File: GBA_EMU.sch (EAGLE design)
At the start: 73 parts, among them J1 USB-MINIB-5PIN, J2 AVR_SPI, Q1 MOSFET-PCHANNEL, SW1 LEFT, SW2 RIGHT, SW3 PWR_SWITCH, U2 FT230X, U4 LM4875, U5 V_REG_LDOSMD2, U7 AZV321, X2 HEADPHONE

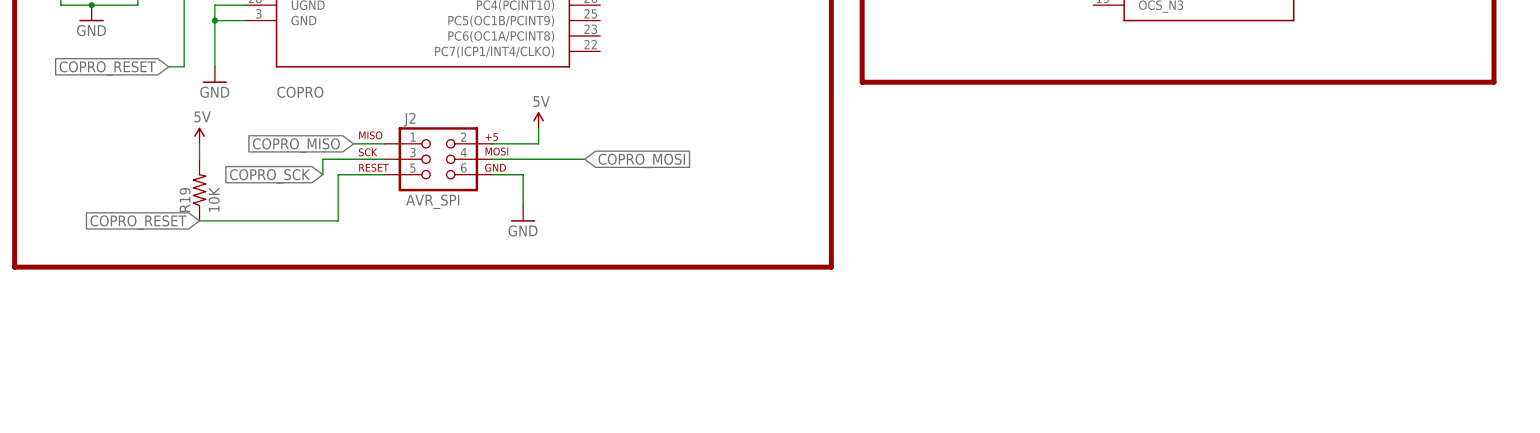
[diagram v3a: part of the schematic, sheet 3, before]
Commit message: added a uSD card slot and a few test points
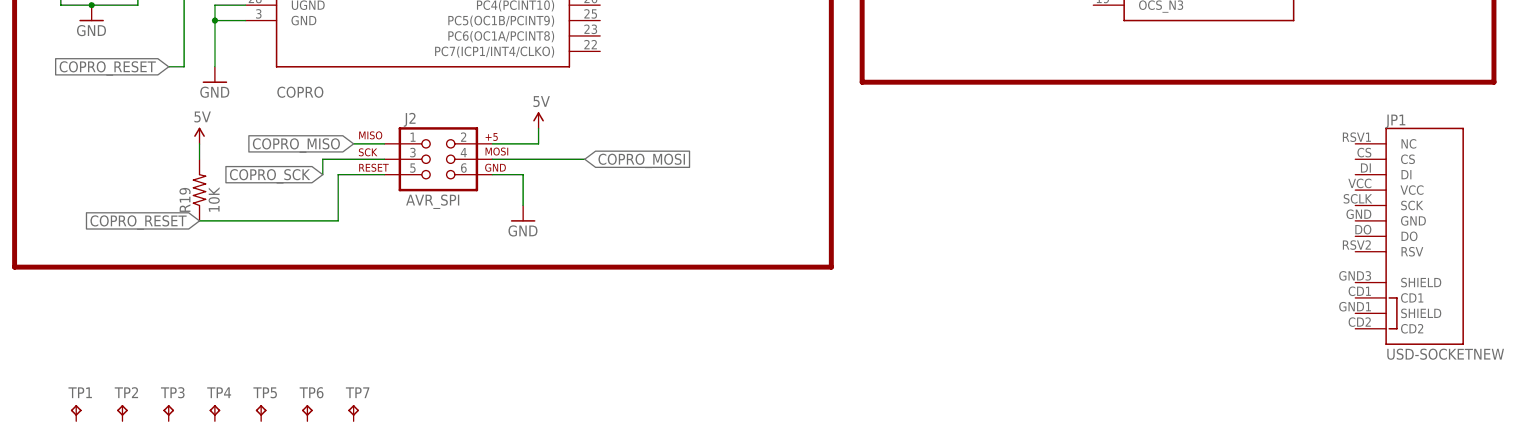
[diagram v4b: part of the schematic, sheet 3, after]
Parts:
- added JP1: USD-SOCKETNEW, SparkFun-Connectors:USD-SOCKETNEW
- added TP1, TP2, TP3, TP4, TP5, TP6, TP7: TPB2,54, testpad:TPB2,54
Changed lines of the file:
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@@
 <part name="GND35" library="SparkFun-Aesthetics" deviceset="GND" device=""/>
 <part name="GND36" library="SparkFun-Aesthetics" deviceset="GND" device=""/>
+<part name="JP1" library="SparkFun-Connectors" deviceset="USD-SOCKET" device="NEW"/>
+<part name="TP1" library="testpad" deviceset="TP" device="B2,54"/>
+<part name="TP2" library="testpad" deviceset="TP" device="B2,54"/>
+<part name="TP3" library="testpad" deviceset="TP" device="B2,54"/>
+<part name="TP4" library="testpad" deviceset="TP" device="B2,54"/>
+<part name="TP5" library="testpad" deviceset="TP" device="B2,54"/>
+<part name="TP6" library="testpad" deviceset="TP" device="B2,54"/>
+<part name="TP7" library="testpad" deviceset="TP" device="B2,54"/>
 </parts>
 <sheets>
@@
 <instance part="SUPPLY21" gate="G$1" x="170.18" y="154.94"/>
 <instance part="GND34" gate="1" x="170.18" y="137.16"/>
+<instance part="JP1" gate="G$1" x="236.22" y="53.34"/>
+<instance part="TP1" gate="G$1" x="17.78" y="22.86"/>
+<instance part="TP2" gate="G$1" x="25.4" y="22.86"/>
+<instance part="TP3" gate="G$1" x="33.02" y="22.86"/>
+<instance part="TP4" gate="G$1" x="40.64" y="22.86"/>
+<instance part="TP5" gate="G$1" x="48.26" y="22.86"/>
+<instance part="TP6" gate="G$1" x="55.88" y="22.86"/>
+<instance part="TP7" gate="G$1" x="63.5" y="22.86"/>
 </instances>
 <busses>

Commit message: added the battery charging circuit
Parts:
- removed D3: DUAL_LED, GBA:DUAL_LED
- removed R12: 620R, rcl:R-EU_R0805
- added B1: (no value), custom:MICROBUILDER_BATTERY
- added C16: 1.0uF, SparkFun-Capacitors:1.0UF-16V-10%(0603)
- added C19: 0.1uF, SparkFun-Capacitors:0.1UF-25V(+80/-20%)(0603)
- added C20: 100uF, SparkFun-Capacitors:CAP_POL1206
- added D1: DUAL_LED, custom:DUAL_LED
- added L2: (no value), custom:MICROBUILDER_INDUCTOR4.9X4.9MM
- added R20: 200k, SparkFun-Resistors:200KOHM1/10W1%(0603)200K
- added R21: 270k, SparkFun-Resistors:200KOHM1/10W1%(0603)200K
- added R22: 100k, SparkFun-Resistors:100KOHM-1/10W-1%(0603)
- added R23, R24: 1K, SparkFun-Resistors:1KOHM-1/10W-1%(0603)
- added U1: (no value), custom:TPS6103X
- added U3: (no value), custom:MCP73871
- TP1, TP2, TP3, TP4, TP5, TP6, TP7: value TPB2,54 -> PTR1TP12R; device testpad:TPB2,54 -> testpad:PTR1TP12R
- U5: value V_REG_LDOSMD2 -> Mic5365-2.8Y
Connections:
- new net N$30: L2.2, U1.SW
- new net N$31: R20.1, U1.EN
- new net N$32: R21.1, R22.2, U3.VPCC
- new net N$33: R24.1, U3.STAT2
- new net N$34: R23.1, U3.STAT1/LBO
- new net N$35: B1.+, U3.VBAT1, U3.VBAT2, U3.VBATSENS
- new net N$36: R23.2
- new net N$37: D1.3, R24.2
- new net N$38: R18.1
- new net V_BATT: C16.1, C19.1, L2.1, R20.2, U1.VBAT
- new net V_USB: D1.4, R21.2, U3.VIN1, U3.VIN2
- net 2.8V: now also TP3.TP
- net 3.3V: now also TP2.TP
- net 5V: now also C20.+, TP1.TP, U1.VOUT
- net A_BTN: now also COPRO.PD4(INT5/AIN3)
- net B_BTN: now also COPRO.PD5(XCK/AIN4/PCINT12)
- net GND: now also B1.-, C16.2, C19.2, C20.-, R22.1, TP4.TP, U$1.GND, U1.GND, U1.SYNC; no longer R12.2
- net N$23: now also R17.1; no longer D3.2, R12.1
- net SELECT: now also COPRO.PD7(INT7/HWB/AIN6/T0)
- net START: now also COPRO.PD6(INT6/AIN5/RTS)
- net Z_BTN: now also COPRO.PB0(SS/PCINT0)
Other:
- note added: "Battery Controller"
- note added: "Boost Converter"
- note added: "TFT Power Generation"
- note removed: "POWER LED INDICATION"

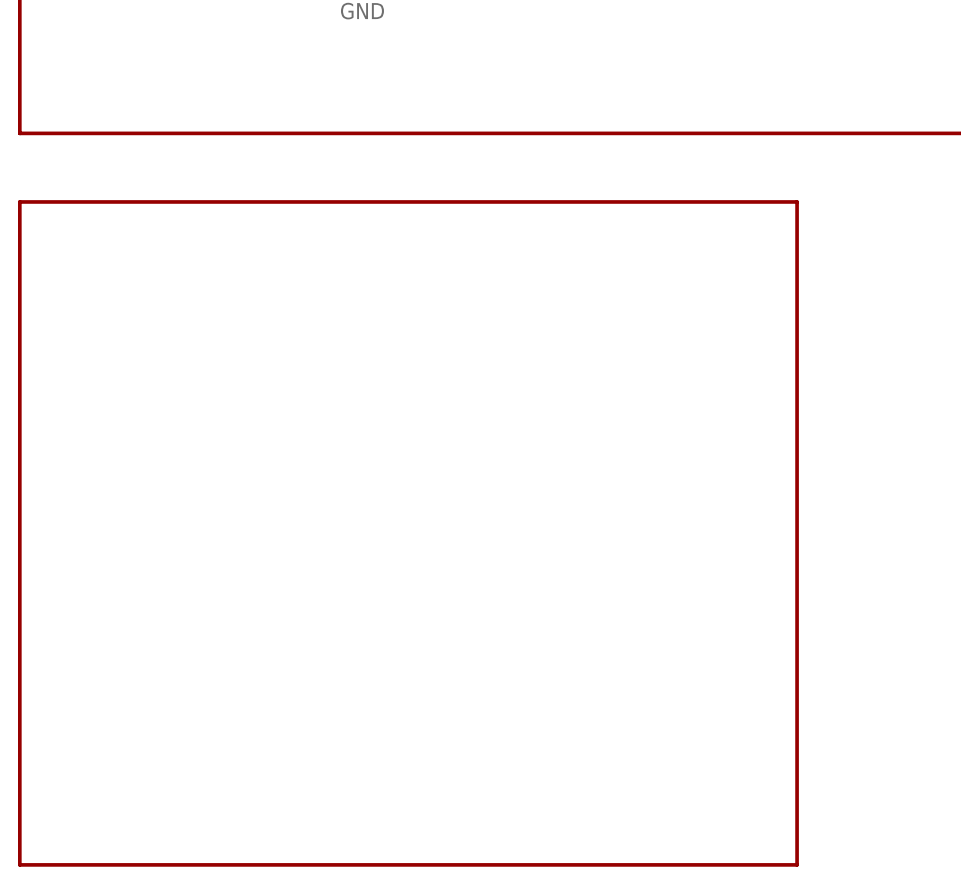
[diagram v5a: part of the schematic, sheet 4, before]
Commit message: added a fan for overheating?
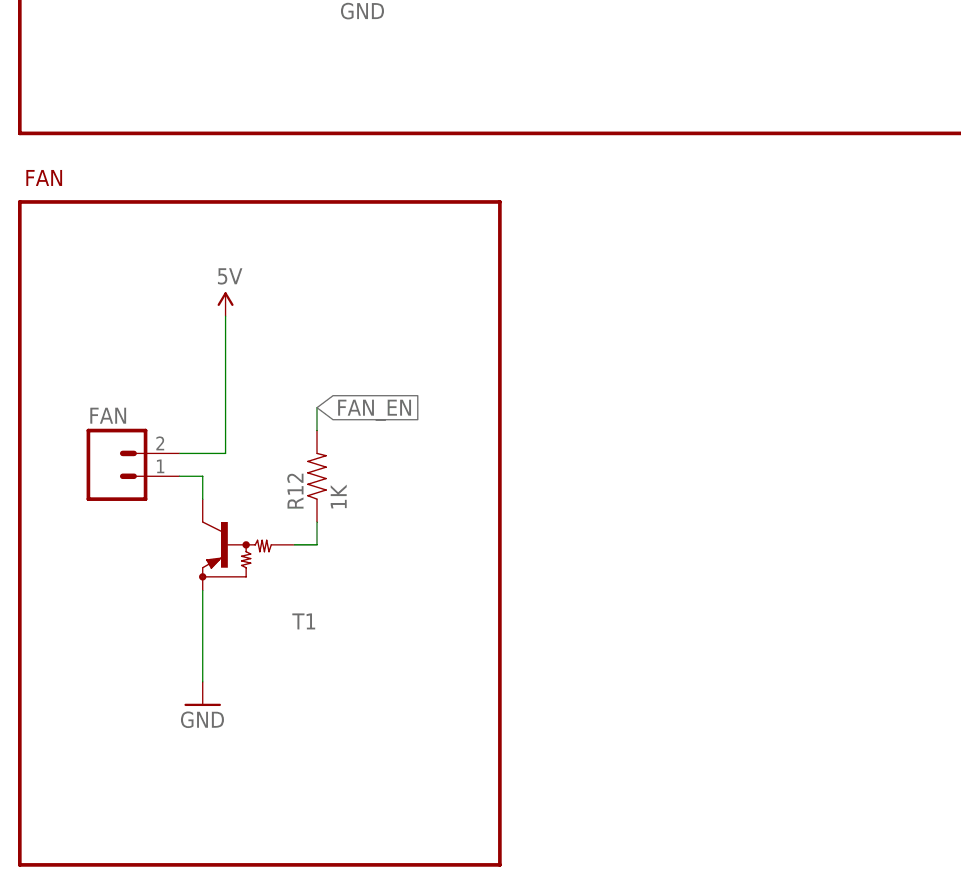
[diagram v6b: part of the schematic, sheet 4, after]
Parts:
- added FAN: (no value), SparkFun-Connectors:M02PTH
- added R12: 1K, SparkFun-Resistors:1KOHM-1/10W-1%(0603)
- added T1: (no value), custom:TRANSISTOR_PNP_DRIVERMUN2111T1SC59-BEC
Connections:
- new net FAN_EN: R12.2
- new net N$39: FAN.1, T1.C
- new net N$40: R12.1, T1.B
- net 5V: now also FAN.2
- net GND: now also T1.E
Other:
- note added: "FAN"
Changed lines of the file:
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@@
 <part name="TP6" library="testpad" deviceset="PTR1" device="TP12R"/>
 <part name="TP7" library="testpad" deviceset="PTR1" device="TP12R"/>
+<part name="FAN" library="SparkFun-Connectors" deviceset="M02" device="PTH"/>
+<part name="SUPPLY33" library="SparkFun-Aesthetics" deviceset="5V" device=""/>
+<part name="GND45" library="SparkFun-Aesthetics" deviceset="GND" device=""/>
+<part name="T1" library="custom" deviceset="TRANSISTOR_PNP_DRIVER" device="SC59-BEC" technology="MUN2111T1"/>
+<part name="R12" library="SparkFun-Resistors" deviceset="1KOHM-1/10W-1%(0603)" device="" value="1K"/>
 </parts>
 <sheets>
@@
 <wire x1="259.08" y1="76.2" x2="259.08" y2="157.48" width="0.4064" layer="94"/>
 <text x="132.08" y="160.02" size="1.778" layer="94">Battery Controller</text>
-<wire x1="0" y1="68.58" x2="86.36" y2="68.58" width="0.4064" layer="94"/>
-<wire x1="86.36" y1="68.58" x2="86.36" y2="-5.08" width="0.4064" layer="94"/>
-<wire x1="86.36" y1="-5.08" x2="0" y2="-5.08" width="0.4064" layer="94"/>
+<wire x1="0" y1="68.58" x2="53.34" y2="68.58" width="0.4064" layer="94"/>
+<wire x1="53.34" y1="68.58" x2="53.34" y2="-5.08" width="0.4064" layer="94"/>
+<wire x1="53.34" y1="-5.08" x2="0" y2="-5.08" width="0.4064" layer="94"/>
 <wire x1="0" y1="-5.08" x2="0" y2="68.58" width="0.4064" layer="94"/>
+<text x="0.508" y="70.358" size="1.778" layer="94">FAN</text>
 </plain>
 <instances>
@@
 <instance part="GND44" gate="1" x="215.9" y="88.9"/>
 <instance part="D1" gate="D$1" x="142.24" y="137.16"/>
+<instance part="FAN" gate="G$1" x="10.16" y="38.1"/>
+<instance part="SUPPLY33" gate="G$1" x="22.86" y="55.88"/>
+<instance part="GND45" gate="1" x="20.32" y="12.7"/>
+<instance part="T1" gate="G$1" x="22.86" y="30.48" rot="R180"/>
+<instance part="R12" gate="G$1" x="33.02" y="38.1" rot="R90"/>
 </instances>
 <busses>
@@
 <pinref part="GND43" gate="1" pin="GND"/>
 </segment>
+<segment>
+<pinref part="T1" gate="G$1" pin="E"/>
+<pinref part="GND45" gate="1" pin="GND"/>
+<wire x1="20.32" y1="25.4" x2="20.32" y2="15.24" width="0.1524" layer="91"/>
+</segment>
 </net>
 <net name="5V" class="0">
@@
 <junction x="109.22" y="137.16"/>
 <pinref part="SUPPLY27" gate="G$1" pin="5V"/>
+</segment>
+<segment>
+<pinref part="SUPPLY33" gate="G$1" pin="5V"/>
+<wire x1="22.86" y1="40.64" x2="22.86" y2="55.88" width="0.1524" layer="91"/>
+<pinref part="FAN" gate="G$1" pin="2"/>
+<wire x1="22.86" y1="40.64" x2="17.78" y2="40.64" width="0.1524" layer="91"/>
 </segment>
 </net>
@@
 </segment>
 </net>
+<net name="N$39" class="0">
+<segment>
+<pinref part="FAN" gate="G$1" pin="1"/>
+<pinref part="T1" gate="G$1" pin="C"/>
+<wire x1="17.78" y1="38.1" x2="20.32" y2="38.1" width="0.1524" layer="91"/>
+<wire x1="20.32" y1="38.1" x2="20.32" y2="35.56" width="0.1524" layer="91"/>
+</segment>
+</net>
+<net name="N$40" class="0">
+<segment>
+<pinref part="T1" gate="G$1" pin="B"/>
+<pinref part="R12" gate="G$1" pin="1"/>
+<wire x1="30.48" y1="30.48" x2="33.02" y2="30.48" width="0.1524" layer="91"/>
+<wire x1="33.02" y1="30.48" x2="33.02" y2="33.02" width="0.1524" layer="91"/>
+</segment>
+</net>
+<net name="FAN_EN" class="0">
+<segment>
+<pinref part="R12" gate="G$1" pin="2"/>
+<wire x1="33.02" y1="43.18" x2="33.02" y2="45.72" width="0.1524" layer="91"/>
+<label x="33.02" y="45.72" size="1.778" layer="95" xref="yes"/>
+</segment>
+</net>
